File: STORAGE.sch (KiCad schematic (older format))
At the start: 10 parts

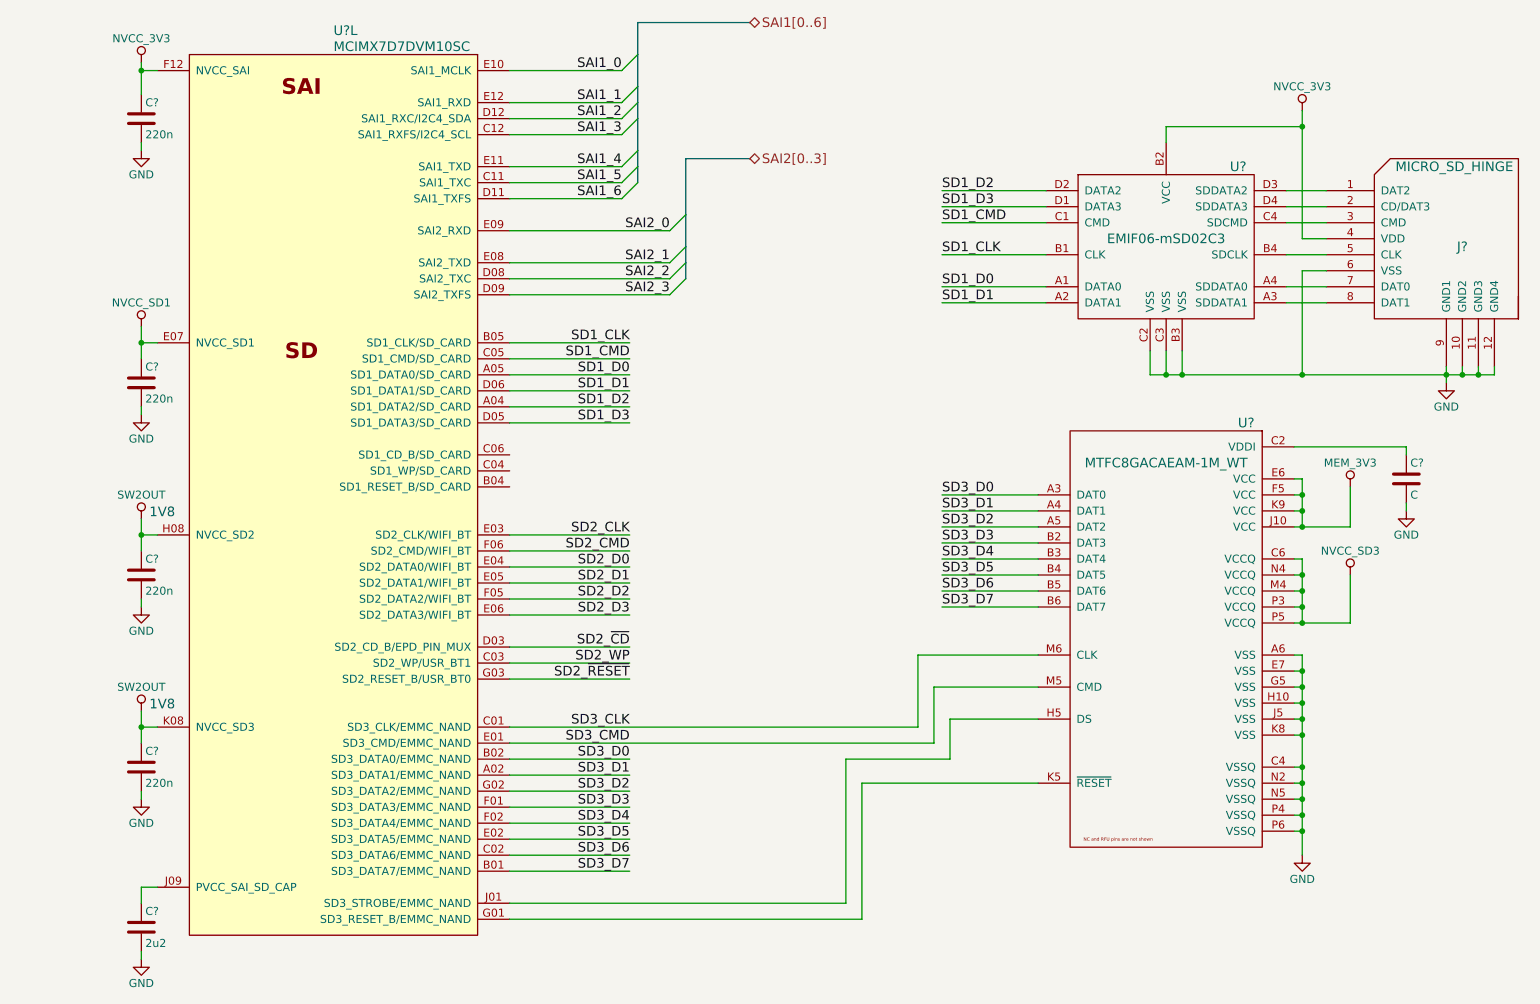
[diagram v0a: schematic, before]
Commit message: Connected WIFI subsheet with ESP8266 and WL1807MOD to SD2 Connected WL1807MOD Bluetoth UART to UART3 Connected A7 Module AT UART to UART6 Connected A7 GPS UART to UART5 Connected A7 HS download to UART7 Connected debug pins to UART1 Connected debug pins to UART2 Added CPU_PWR subsheet to connect power rails to i.MX7 A7 UARTs are routed through level shifter to get from 2.8V to 3.3V All the sheets should be on A3 size now Externel USB is connected to USB_OTG1 Board power sheet is cleared out. Only 4V booster is needed.
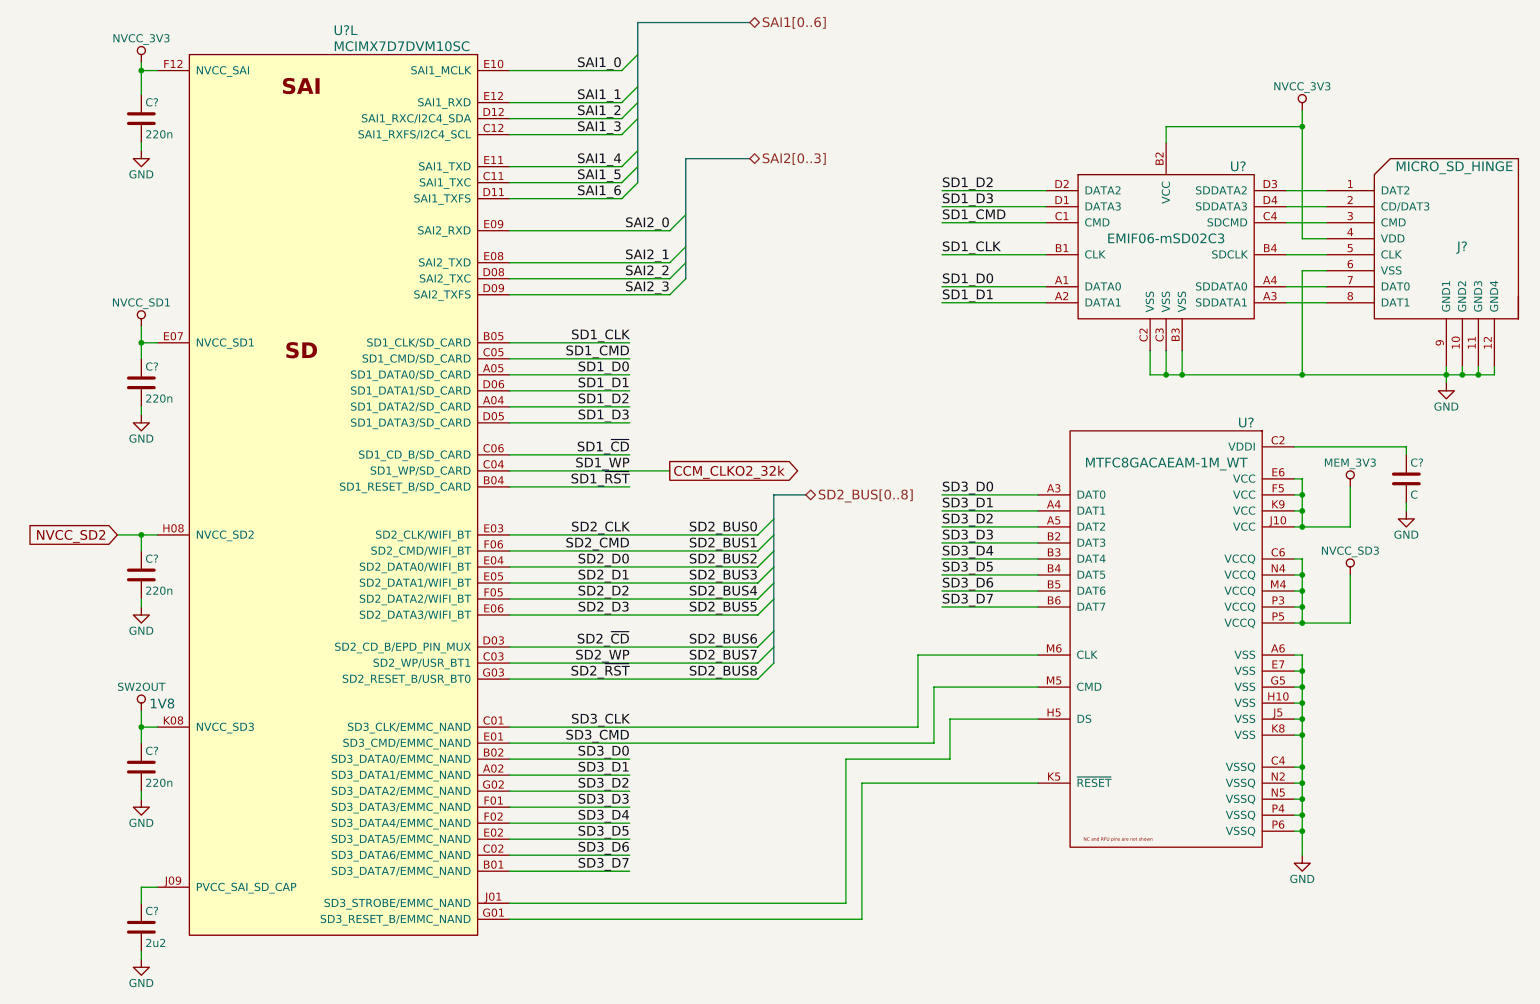
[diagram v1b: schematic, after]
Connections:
- net SW2OUT: no longer C?.1, U?.H08 (NVCC_SD2)
- net SD1_~RST: now reaches U?.B04 (SD1_RESET_B/SD_CARD)
- net CCM_CLKO2_32k: now reaches U?.C04 (SD1_WP/SD_CARD)
- net SD1_~CD: now reaches U?.C06 (SD1_CD_B/SD_CARD)
- net SD2_CLK renamed SD2_BUS0
- net SD2_CMD renamed SD2_BUS1
- net SD2_D0 renamed SD2_BUS2
- net SD2_D1 renamed SD2_BUS3
- net SD2_D2 renamed SD2_BUS4
- net SD2_D3 renamed SD2_BUS5
- net SD2_WP renamed SD2_BUS7
- net SD2_~CD renamed SD2_BUS6
- net SD2_~RESET renamed SD2_BUS8
- new net NVCC_SD2: C?.1, U?.H08 (NVCC_SD2)
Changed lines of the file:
@@
 LIBS:emif06-msd02c3
 LIBS:mtfc8gacaeam-1m_wt
+LIBS:sn74avc2t244
 LIBS:3210retro-cache
 EELAYER 25 0
@@
 $Descr A4 11693 8268
 encoding utf-8
-Sheet 11 11
-Title ""
-Date ""
-Rev ""
-Comp ""
-Comment1 ""
+Sheet 11 12
+Title "Nokia 3210 Retrofit"
+Date "2017-06-15"
+Rev "2"
+Comp "www.kurzschluss-blog.de"
+Comment1 "Retrofitting board for Nokia 3210 mobile phone"
 Comment2 ""
 Comment3 ""
@@
 SAI2_0
 Wire Bus Line
-	4950 900  4950 1100
-Wire Bus Line
-	4950 1100 4950 1300
-Wire Bus Line
-	4950 1300 4950 1400
-Wire Bus Line
-	4950 1400 4950 1500
-Wire Bus Line
-	4950 1500 4950 1700
-Wire Bus Line
-	4950 1700 4950 1800
-Wire Bus Line
-	4950 1800 4950 1900
+	4950 900  4950 1900
 Wire Bus Line
 	4950 900  5650 900
 Wire Bus Line
-	5250 1750 5250 2100
-Wire Bus Line
-	5250 2100 5250 2300
-Wire Bus Line
-	5250 2300 5250 2400
-Wire Bus Line
-	5250 2400 5250 2500
+	5250 1750 5250 2500
 Wire Bus Line
 	5250 1750 5650 1750
@@
 $EndComp
 Wire Wire Line
-	10000 3050 10000 3100
-Wire Wire Line
-	10000 3100 10000 3150
-Wire Wire Line
-	8150 3100 8250 3100
-Wire Wire Line
-	8250 3100 8350 3100
-Wire Wire Line
-	8350 3100 9100 3100
-Wire Wire Line
-	9100 3100 10000 3100
-Wire Wire Line
-	10000 3100 10100 3100
-Wire Wire Line
-	10100 3100 10200 3100
-Wire Wire Line
-	10200 3100 10300 3100
+	10000 3050 10000 3150
+Wire Wire Line
+	8150 3100 10300 3100
 Wire Wire Line
 	10300 3100 10300 3050
@@
 	9100 2250 9250 2250
 Wire Wire Line
-	9100 1450 9100 1550
-Wire Wire Line
-	9100 1550 9100 2250
+	9100 1450 9100 2250
 Wire Wire Line
 	9100 1550 8250 1550
@@
 	9400 4050 9400 3800
 Wire Wire Line
-	9050 4050 9100 4050
-Wire Wire Line
-	9100 4050 9400 4050
-Wire Wire Line
-	9100 3750 9100 3850
-Wire Wire Line
-	9100 3850 9100 3950
-Wire Wire Line
-	9100 3950 9100 4050
+	9050 4050 9400 4050
+Wire Wire Line
+	9100 3750 9100 4050
 Wire Wire Line
 	9100 3750 9050 3750
@@
 	9050 4250 9100 4250
 Wire Wire Line
-	9100 4250 9100 4350
-Wire Wire Line
-	9100 4350 9100 4450
-Wire Wire Line
-	9100 4450 9100 4550
-Wire Wire Line
-	9100 4550 9100 4650
-Wire Wire Line
-	9050 4650 9100 4650
-Wire Wire Line
-	9100 4650 9400 4650
+	9100 4250 9100 4650
+Wire Wire Line
+	9050 4650 9400 4650
 Wire Wire Line
 	9050 4550 9100 4550
@@
 	9050 4850 9100 4850
 Wire Wire Line
-	9100 4850 9100 4950
-Wire Wire Line
-	9100 4950 9100 5050
-Wire Wire Line
-	9100 5050 9100 5150
-Wire Wire Line
-	9100 5150 9100 5250
-Wire Wire Line
-	9100 5250 9100 5350
-Wire Wire Line
-	9100 5350 9100 5550
-Wire Wire Line
-	9100 5550 9100 5650
-Wire Wire Line
-	9100 5650 9100 5750
-Wire Wire Line
-	9100 5750 9100 5850
-Wire Wire Line
-	9100 5850 9100 5950
-Wire Wire Line
-	9100 5950 9100 6100
+	9100 4850 9100 6100
 Wire Wire Line
 	9050 4950 9100 4950
@@
 	1950 1200 1850 1200
 Wire Wire Line
-	1850 1150 1850 1200
-Wire Wire Line
-	1850 1200 1850 1350
+	1850 1150 1850 1350
 $Comp
 L NVCC_3V3 #PWR?
@@
 $EndComp
 Wire Wire Line
-	1850 4000 1850 4100
-Wire Wire Line
 	1850 4100 1850 4200
 $Comp
@@
 $EndComp
 Wire Wire Line
-	1850 2800 1850 2900
-Wire Wire Line
-	1850 2900 1850 3000
+	1850 2800 1850 3000
 $Comp
 L GND #PWR?
@@
 $EndComp
 Wire Wire Line
-	1850 5200 1850 5300
-Wire Wire Line
-	1850 5300 1850 5400
+	1850 5200 1850 5400
 $Comp
 L GND #PWR?
@@
 Connection ~ 1850 5300
 Wire Wire Line
-	1950 4100 1850 4100
+	1700 4100 1950 4100
 Connection ~ 1850 4100
 Wire Wire Line
@@
 1V8
 $Comp
-L SW2OUT #PWR?
-U 1 1 5944FEFA
-P 1850 4000
-F 0 "#PWR?" H 1850 3850 50  0001 C CNN
-F 1 "SW2OUT" H 1850 4150 50  0000 C CNN
-F 2 "" H 1850 4000 50  0001 C CNN
-F 3 "" H 1850 4000 50  0001 C CNN
-	1    1850 4000
-	1    0    0    -1
-$EndComp
-Text Notes 1900 4000 0    60   ~ 0
-1V8
-$Comp
 L NVCC_SD1 #PWR?
 U 1 1 594500AD
@@
 $EndComp
 Wire Wire Line
-	4150 4100 4900 4100
-Wire Wire Line
-	4150 4200 4900 4200
-Wire Wire Line
-	4150 4300 4900 4300
-Wire Wire Line
-	4150 4400 4900 4400
-Wire Wire Line
-	4150 4500 4900 4500
-Wire Wire Line
-	4150 4600 4900 4600
-Wire Wire Line
-	4150 5000 4900 5000
-Wire Wire Line
-	4150 4800 4900 4800
-Wire Wire Line
-	4150 4900 4900 4900
+	4150 4100 5700 4100
+Wire Wire Line
+	4150 4200 5700 4200
+Wire Wire Line
+	4150 4300 5700 4300
+Wire Wire Line
+	4150 4400 5700 4400
+Wire Wire Line
+	4150 4500 5700 4500
+Wire Wire Line
+	4150 4600 5700 4600
+Wire Wire Line
+	4150 5000 5700 5000
+Wire Wire Line
+	4150 4800 5700 4800
+Wire Wire Line
+	4150 4900 5700 4900
 Text Label 4900 4300 2    60   ~ 0
 SD2_D0
@@
 SD2_WP
 Text Label 4900 5000 2    60   ~ 0
-SD2_~RESET
+SD2_~RST
+Wire Wire Line
+	4150 3800 4900 3800
+Wire Wire Line
+	4150 3700 5150 3700
+Wire Wire Line
+	4150 3600 4900 3600
+Text Label 4900 3600 2    60   ~ 0
+SD1_~CD
+Text Label 4900 3700 2    60   ~ 0
+SD1_WP
+Text Label 4900 3800 2    60   ~ 0
+SD1_~RST
+Text HLabel 6000 3850 2    60   BiDi ~ 0
+SD2_BUS[0..8]
+Text Label 5700 4100 2    60   ~ 0
+SD2_BUS0
+Text Label 5700 4200 2    60   ~ 0
+SD2_BUS1
+Text Label 5700 4300 2    60   ~ 0
+SD2_BUS2
+Text Label 5700 4400 2    60   ~ 0
+SD2_BUS3
+Text Label 5700 4500 2    60   ~ 0
+SD2_BUS4
+Text Label 5700 4600 2    60   ~ 0
+SD2_BUS5
+Text Label 5700 4800 2    60   ~ 0
+SD2_BUS6
+Text Label 5700 4900 2    60   ~ 0
+SD2_BUS7
+Text Label 5700 5000 2    60   ~ 0
+SD2_BUS8
+Entry Wire Line
+	5700 4100 5800 4000
+Entry Wire Line
+	5700 4200 5800 4100
+Entry Wire Line
+	5700 4300 5800 4200
+Entry Wire Line
+	5700 4400 5800 4300
+Entry Wire Line
+	5700 4500 5800 4400
+Entry Wire Line
+	5700 4600 5800 4500
+Entry Wire Line
+	5700 5000 5800 4900
+Entry Wire Line
+	5700 4800 5800 4700
+Entry Wire Line
+	5700 4900 5800 4800
+Wire Bus Line
+	5800 3850 5800 4900
+Wire Bus Line
+	5800 3850 6000 3850
+Text GLabel 1700 4100 0    60   Input ~ 0
+NVCC_SD2
+Text GLabel 5150 3700 2    60   Output ~ 0
+CCM_CLKO2_32k
 $EndSCHEMATC
